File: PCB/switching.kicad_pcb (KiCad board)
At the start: 4 copper layers, 109.8 x 37.9 mm, 32 parts, among them J1 CURRENT, J2 24VAC, J3 3V3, U1 BD9G101G

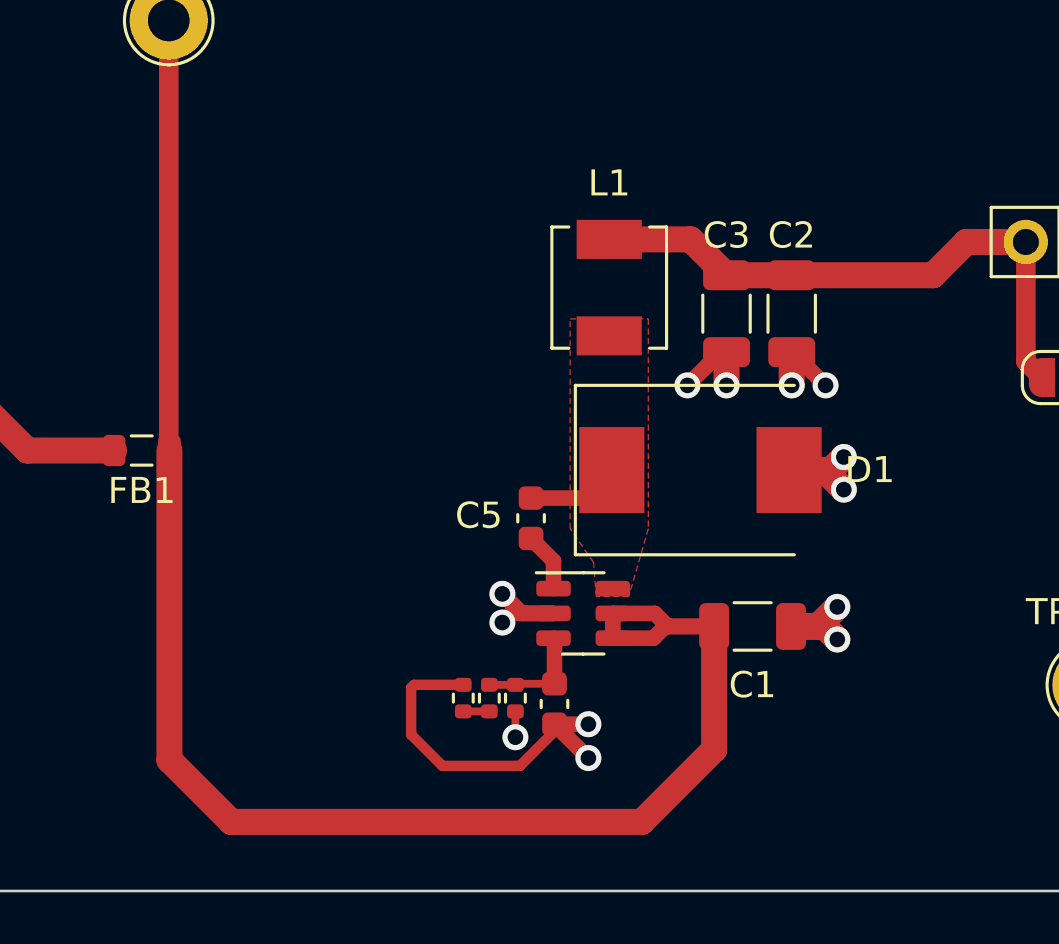
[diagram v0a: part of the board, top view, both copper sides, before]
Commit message: change barrier diode
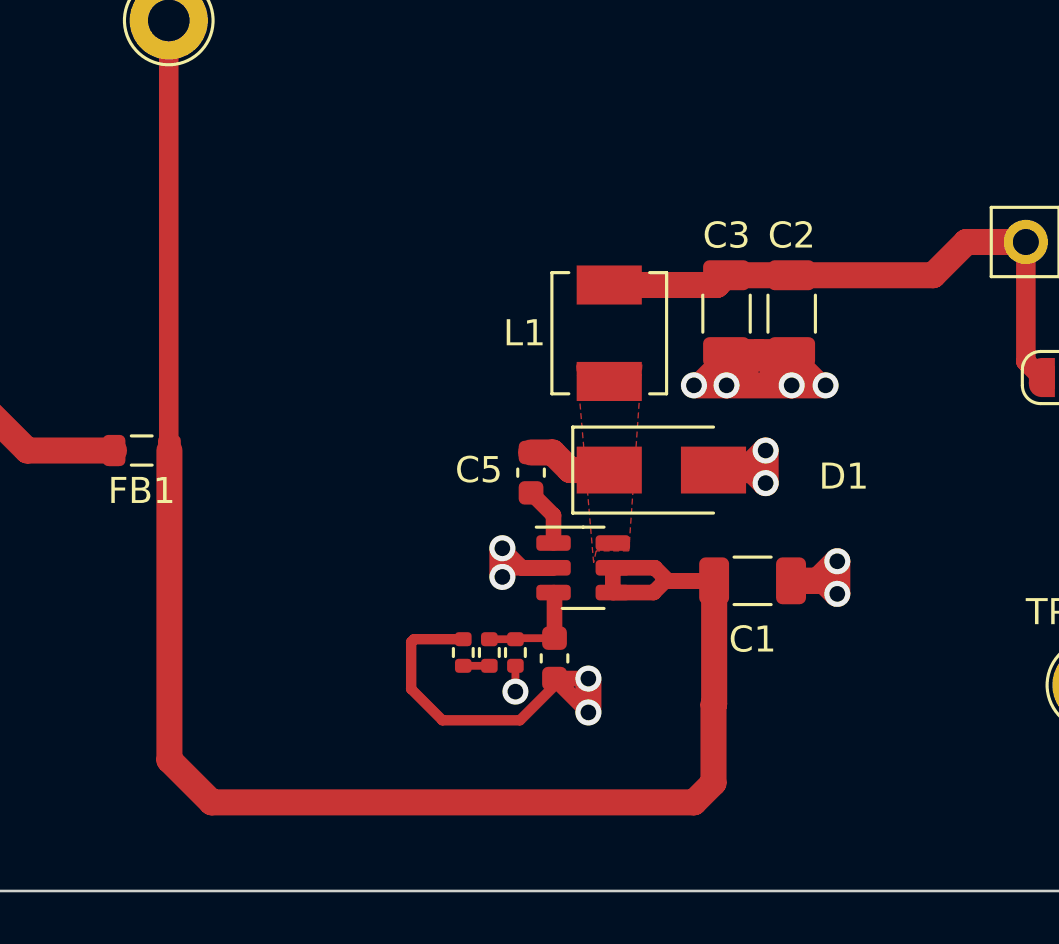
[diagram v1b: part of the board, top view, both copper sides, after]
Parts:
- D1: value SS36-E3/57T -> SS210; footprint Diode_SMD:D_SMC -> Diode_SMD:D_SMA
- moved C1 1.75 mm to (103.0, 73.0)
- moved C4 1.75 mm to (95.4, 76.0)
- moved C5 1.75 mm to (94.5, 68.8)
- moved L1 1.75 mm to (97.5, 63.5)
- moved R11 1.75 mm to (91.9, 75.8)
- moved R12 1.75 mm to (92.9, 75.8)
- moved R2 1.75 mm to (93.9, 75.8)
- moved U1 1.75 mm to (96.5, 72.5)
- moved D1 1.50 mm to (99.5, 68.8)
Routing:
- net GND: track 29.9 -> 44.1 mm
- net Net-(C1-Pad1): track 65.3 -> 67.1 mm
- net +3.3V: track 36.3 -> 37.2 mm

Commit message: silkscreen changes for v1
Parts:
- moved TP2 6.60 mm to (47.2, 54.8)
- moved TP3 4.36 mm to (83.5, 54.8)
- moved C1 1.25 mm to (101.8, 73.0)
- moved C2 0.25 mm to (104.5, 63.0)
- moved C3 0.25 mm to (102.0, 63.0)
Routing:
- net Net-(C1-Pad1): track 67.1 -> 59.1 mm
- net Net-(D2-Pad1): track 38.6 -> 37.7 mm
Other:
- board text added: "switching v1"

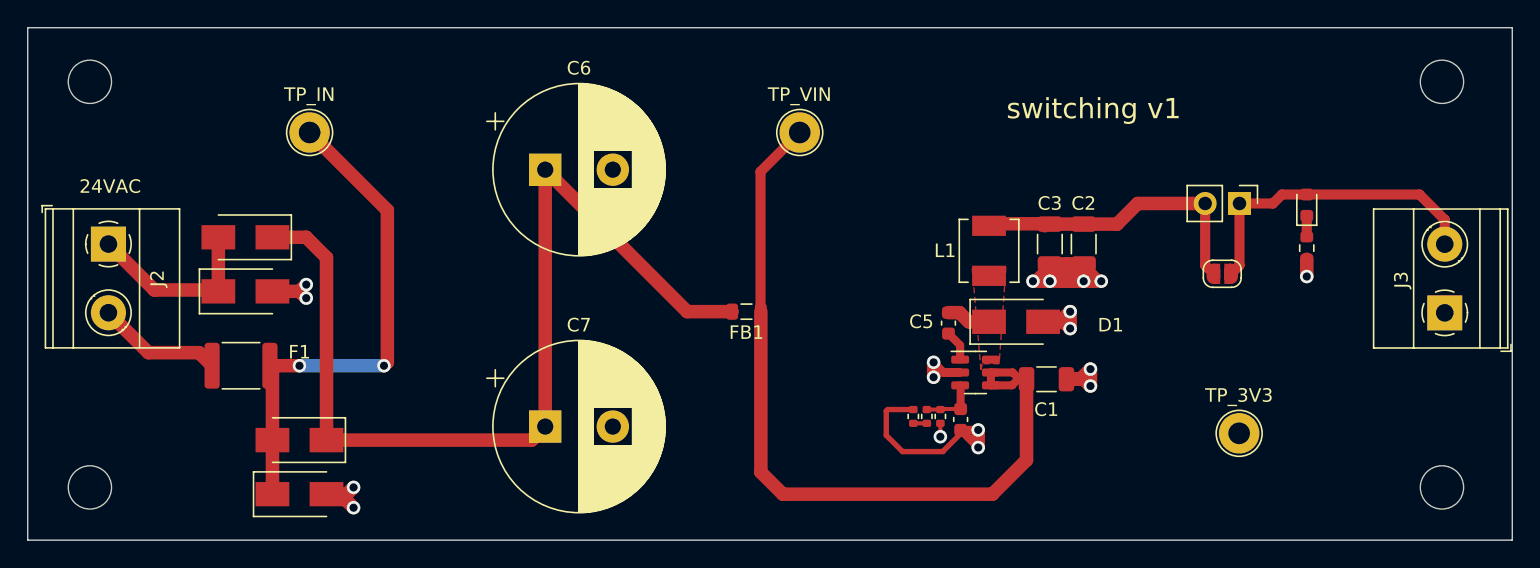
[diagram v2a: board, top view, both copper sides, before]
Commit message: convert to 2 layer
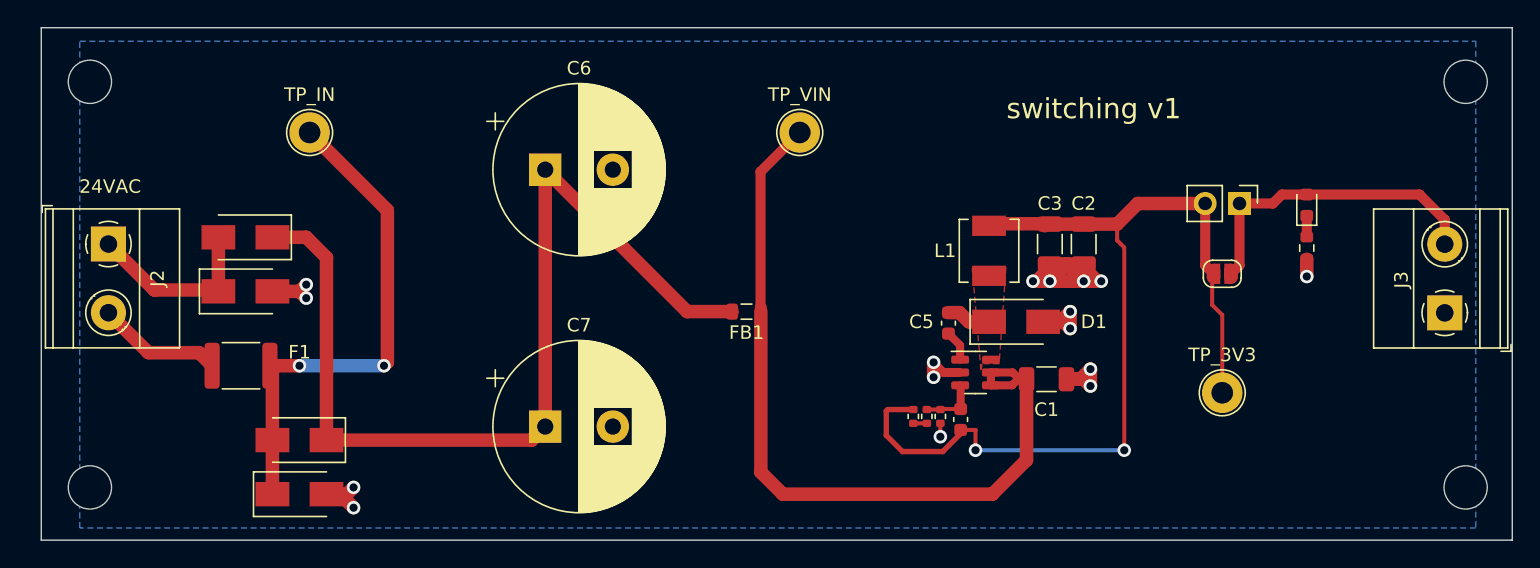
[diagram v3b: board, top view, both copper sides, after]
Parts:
- moved TP4 3.25 mm to (114.8, 74.0)
- moved H1 1.75 mm to (132.8, 81.0)
- moved H4 1.75 mm to (132.8, 51.0)
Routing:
- net +3.3V: track 36.9 -> 72.2 mm
- added copper zone on B.Cu, net GND
- removed copper zone on In2.Cu, net +3.3V
- removed copper zone on In1.Cu, net GND
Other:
- board size 109.8 x 37.9 mm -> 108.8 x 37.9 mm
- copper layers 4 -> 2
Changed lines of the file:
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@@
 (kicad_pcb (version 20211014) (generator pcbnew)
   (general
-    (thickness 4.69)
+    (thickness 1.6)
   )
   (paper "A4")
   (layers
     (0 "F.Cu" signal)
-    (1 "In1.Cu" power)
-    (2 "In2.Cu" power)
     (31 "B.Cu" signal)
     (32 "B.Adhes" user "B.Adhesive")
@@
       (layer "F.Cu" (type "copper") (thickness 0.035))
       (layer "dielectric 1" (type "core") (thickness 1.51) (material "FR4") (epsilon_r 4.5) (loss_tangent 0.02))
-      (layer "In1.Cu" (type "copper") (thickness 0.035))
-      (layer "dielectric 2" (type "prepreg") (thickness 1.51) (material "FR4") (epsilon_r 4.5) (loss_tangent 0.02))
-      (layer "In2.Cu" (type "copper") (thickness 0.035))
-      (layer "dielectric 3" (type "core") (thickness 1.51) (material "FR4") (epsilon_r 4.5) (loss_tangent 0.02))
       (layer "B.Cu" (type "copper") (thickness 0.035))
       (layer "B.Mask" (type "Bottom Solder Mask") (thickness 0.01))
@@
   (net 11 "/LX")
   (net 12 "Net-(C1-Pad1)")
-  (net 13 "Net-(J1-Pad1)")
+  (net 13 "Net-(D6-Pad2)")
   (footprint "MountingHole:MountingHole_3.2mm_M3" (layer "F.Cu")
-    (at 131 51)
+    (at 132.75 51)
     (descr "Mounting Hole 3.2mm, no annular, M3")
     (tags "mounting hole 3.2mm no annular m3")
@@
       (net 1 "GND") (pinfunction "Pin_1") (pintype "passive"))
     (pad "2" thru_hole circle (at 5.08 0 90) (size 2.6 2.6) (drill 1.3) (layers *.Cu *.Mask)
-      (net 13 "Net-(J1-Pad1)") (pinfunction "Pin_2") (pintype "passive"))
+      (net 13 "Net-(D6-Pad2)") (pinfunction "Pin_2") (pintype "passive"))
     (model "${KICAD6_3DMODEL_DIR}/TerminalBlock_Phoenix.3dshapes/TerminalBlock_Phoenix_MKDS-1,5-2-5.08_1x02_P5.08mm_Horizontal.wrl"
       (offset (xyz 0 0 0))
@@
       ))
     (pad "2" smd custom (at 0.65 0) (size 1 0.5) (layers "F.Cu" "F.Mask")
-      (net 13 "Net-(J1-Pad1)") (pinfunction "B") (pintype "passive") (zone_connect 2)
+      (net 13 "Net-(D6-Pad2)") (pinfunction "B") (pintype "passive") (zone_connect 2)
       (options (clearance outline) (anchor rect))
       (primitives
@@
   )
   (footprint "TestPoint:TestPoint_Loop_D2.60mm_Drill1.6mm_Beaded" (layer "F.Cu")
-    (at 116 77)
+    (at 114.75 74)
     (descr "wire loop with bead as test point, loop diameter2.6mm, hole diameter 1.6mm")
     (tags "test point wire loop bead")
@@
     (property "Sheetname" "")
     (attr smd)
-    (fp_text reference "D1" (at 7 0.25) (layer "F.SilkS")
+    (fp_text reference "D1" (at 5.75 0) (layer "F.SilkS")
       (effects (font (size 1 1) (thickness 0.15)))
     )
@@
     (fp_line (start 1.27 3.81) (end -1.27 3.81) (layer "F.Fab") (width 0.1))
     (pad "1" thru_hole rect (at 0 0 270) (size 1.7 1.7) (drill 1) (layers *.Cu *.Mask)
-      (net 13 "Net-(J1-Pad1)") (pinfunction "Pin_1") (pintype "passive"))
+      (net 13 "Net-(D6-Pad2)") (pinfunction "Pin_1") (pintype "passive"))
     (pad "2" thru_hole oval (at 0 2.54 270) (size 1.7 1.7) (drill 1) (layers *.Cu *.Mask)
       (net 6 "+3.3V") (pinfunction "Pin_2") (pintype "passive"))
@@
       (net 5 "Net-(D6-Pad1)") (pinfunction "K") (pintype "passive"))
     (pad "2" smd roundrect (at 0.7875 0 90) (size 0.875 0.95) (layers "F.Cu" "F.Paste" "F.Mask") (roundrect_rratio 0.25)
-      (net 13 "Net-(J1-Pad1)") (pinfunction "A") (pintype "passive"))
+      (net 13 "Net-(D6-Pad2)") (pinfunction "A") (pintype "passive"))
     (model "${KICAD6_3DMODEL_DIR}/LED_SMD.3dshapes/LED_0603_1608Metric.wrl"
       (offset (xyz 0 0 0))
@@
   )
   (footprint "MountingHole:MountingHole_3.2mm_M3" (layer "F.Cu")
-    (at 131 81)
+    (at 132.75 81)
     (descr "Mounting Hole 3.2mm, no annular, M3")
     (tags "mounting hole 3.2mm no annular m3")
@@
     (pad "" np_thru_hole circle (at 0 0) (size 3.2 3.2) (drill 3.2) (layers *.Cu *.Mask))
   )
-  (gr_rect (start 26.4 47) (end 136.2 84.9) (layer "Edge.Cuts") (width 0.1) (fill none))
+  (gr_rect (start 27.4 47) (end 136.2 84.9) (layer "Edge.Cuts") (width 0.1) (fill none))
   (gr_text "switching v1" (at 105.25 53) (layer "F.SilkS")
     (effects (font (size 1.5 1.5) (thickness 0.3)))
@@
   (segment (start 89.9 75.35) (end 90.01 75.24) (width 0.4) (layer "F.Cu") (net 6))
   (segment (start 101.475 61.5) (end 101.625 61.65) (width 1) (layer "F.Cu") (net 6))
+  (segment (start 106.975 62.725) (end 107.25 63) (width 0.3) (layer "F.Cu") (net 6))
   (segment (start 108.5 60) (end 113.485 60) (width 1) (layer "F.Cu") (net 6))
-  (segment (start 96.7 78.05) (end 96.7 76.75) (width 1) (layer "F.Cu") (net 6))
+  (segment (start 114.75 68.25) (end 114 67.5) (width 0.3) (layer "F.Cu") (net 6))
+  (segment (start 96.5 78.25) (end 96.5 76.75) (width 0.3) (layer "F.Cu") (net 6))
   (segment (start 94.072793 78.35) (end 91.1 78.35) (width 0.4) (layer "F.Cu") (net 6))
   (segment (start 89.9 77.15) (end 89.9 75.35) (width 0.4) (layer "F.Cu") (net 6))
@@
   (segment (start 95.4 76.75) (end 95.4 77.022793) (width 0.4) (layer "F.Cu") (net 6))
   (segment (start 102 61.525) (end 104.5 61.525) (width 1) (layer "F.Cu") (net 6))
-  (segment (start 95.4 76.75) (end 96.7 78.05) (width 0.6) (layer "F.Cu") (net 6))
+  (segment (start 107.5 63.25) (end 107.5 78.25) (width 0.3) (layer "F.Cu") (net 6))
+  (segment (start 114.75 74) (end 114.75 68.25) (width 0.3) (layer "F.Cu") (net 6))
+  (segment (start 96.5 76.75) (end 95.4 76.75) (width 0.3) (layer "F.Cu") (net 6))
   (segment (start 90.01 75.24) (end 91.9 75.24) (width 0.4) (layer "F.Cu") (net 6))
+  (segment (start 106.975 61.525) (end 106.975 62.725) (width 0.3) (layer "F.Cu") (net 6))
+  (segment (start 114 67.5) (end 114 65.3) (width 0.3) (layer "F.Cu") (net 6))
   (segment (start 91.1 78.35) (end 89.9 77.15) (width 0.4) (layer "F.Cu") (net 6))
+  (segment (start 114 65.3) (end 114.1 65.2) (width 0.3) (layer "F.Cu") (net 6))
   (segment (start 97.65 61.5) (end 101.475 61.5) (width 1) (layer "F.Cu") (net 6))
-  (segment (start 95.4 76.75) (end 96.7 76.75) (width 0.6) (layer "F.Cu") (net 6))
+  (segment (start 107.25 63) (end 107.5 63.25) (width 0.3) (layer "F.Cu") (net 6))
   (segment (start 97.5 61.65) (end 97.65 61.5) (width 1) (layer "F.Cu") (net 6))
   (segment (start 113.485 60) (end 113.485 64.585) (width 0.75) (layer "F.Cu") (net 6))
   (segment (start 113.485 64.585) (end 114.1 65.2) (width 0.75) (layer "F.Cu") (net 6))
-  (via (at 96.7 76.75) (size 1) (drill 0.6) (layers "F.Cu" "B.Cu") (net 6))
-  (via (at 96.7 78.05) (size 1) (drill 0.6) (layers "F.Cu" "B.Cu") (net 6))
+  (via (at 107.5 78.25) (size 1) (drill 0.6) (layers "F.Cu" "B.Cu") (net 6))
+  (via (at 96.5 78.25) (size 1) (drill 0.6) (layers "F.Cu" "B.Cu") (net 6))
+  (segment (start 96.5 78.25) (end 107.5 78.25) (width 0.3) (layer "B.Cu") (net 6))
   (segment (start 35.326041 71.035) (end 39.073541 71.035) (width 1) (layer "F.Cu") (net 7))
   (segment (start 39.073541 71.035) (end 40.038541 72) (width 1) (layer "F.Cu") (net 7))
@@
     )
   )
-  (zone (net 1) (net_name "GND") (layer "In1.Cu") (hatch edge 0.508)
+  (zone (net 1) (net_name "GND") (layer "B.Cu") (hatch edge 0.508)
     (connect_pads (clearance 0.508))
     (min_thickness 0.254) (filled_areas_thickness no)
-    (fill yes (thermal_gap 0.508) (thermal_bridge_width 0.508))
+    (fill yes (thermal_gap 0.508) (thermal_bridge_width 0.508) (smoothing fillet) (radius 2))
     (polygon
       (pts
-        (xy 177 152)
-        (xy 27 152)
-        (xy 27 46)
-        (xy 177 46)
+        (xy 133.5 84)
+        (xy 30.25 84)
+        (xy 30.25 48)
+        (xy 133.5 48)
       )
     )
-  )
-  (zone (net 6) (net_name "+3.3V") (layer "In2.Cu") (hatch edge 0.508)
-    (connect_pads (clearance 0.508))
-    (min_thickness 0.254) (filled_areas_thickness no)
-    (fill yes (thermal_gap 0.508) (thermal_bridge_width 0.508))
-    (polygon
-      (pts
-        (xy 177 152)
-        (xy 27 152)
-        (xy 27 46)
-        (xy 177 46)
-      )
-    )
